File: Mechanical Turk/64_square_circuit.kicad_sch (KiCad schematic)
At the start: 82 parts, among them U1 LM2596S-ADJ

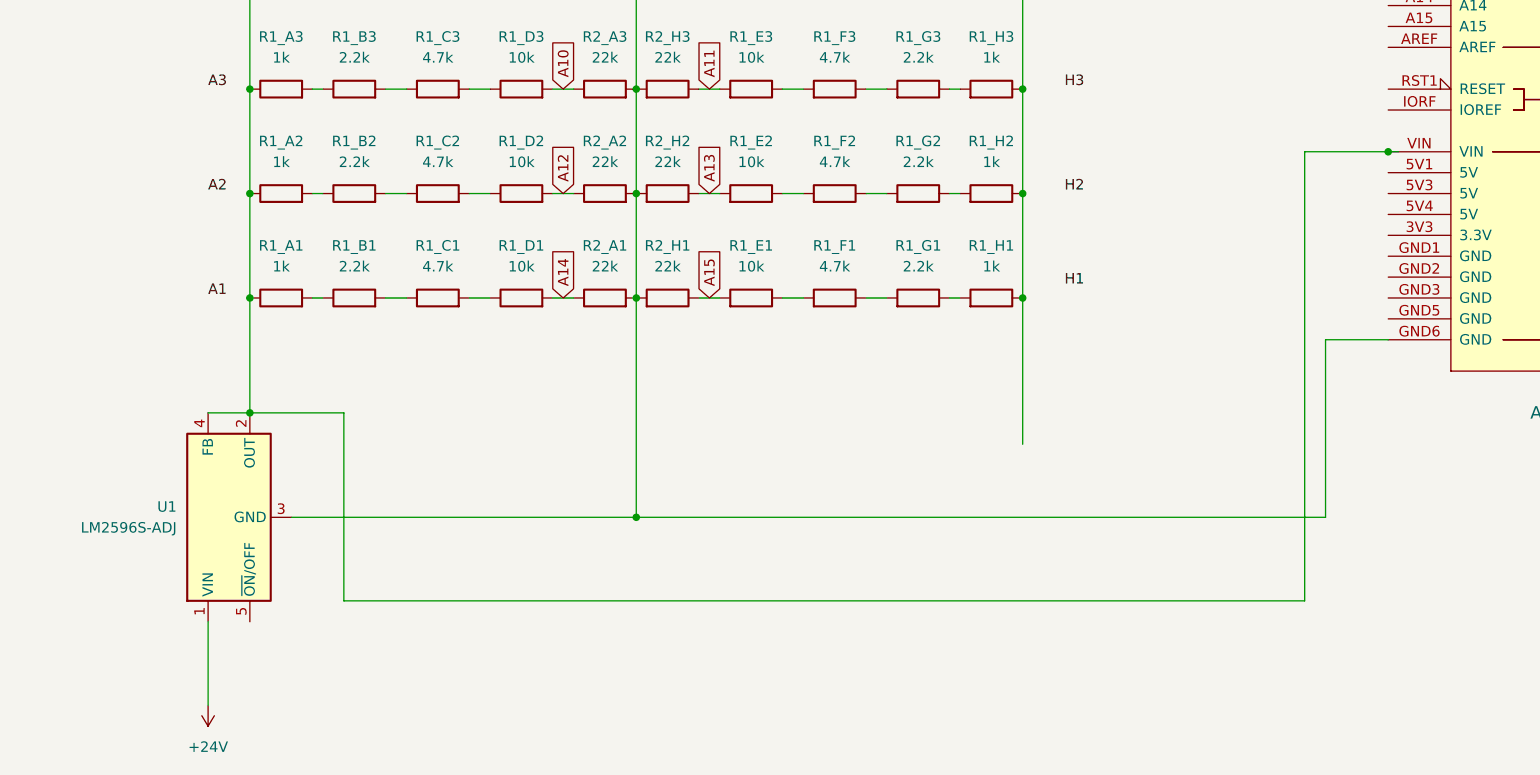
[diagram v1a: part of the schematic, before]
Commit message: gripper design is completed
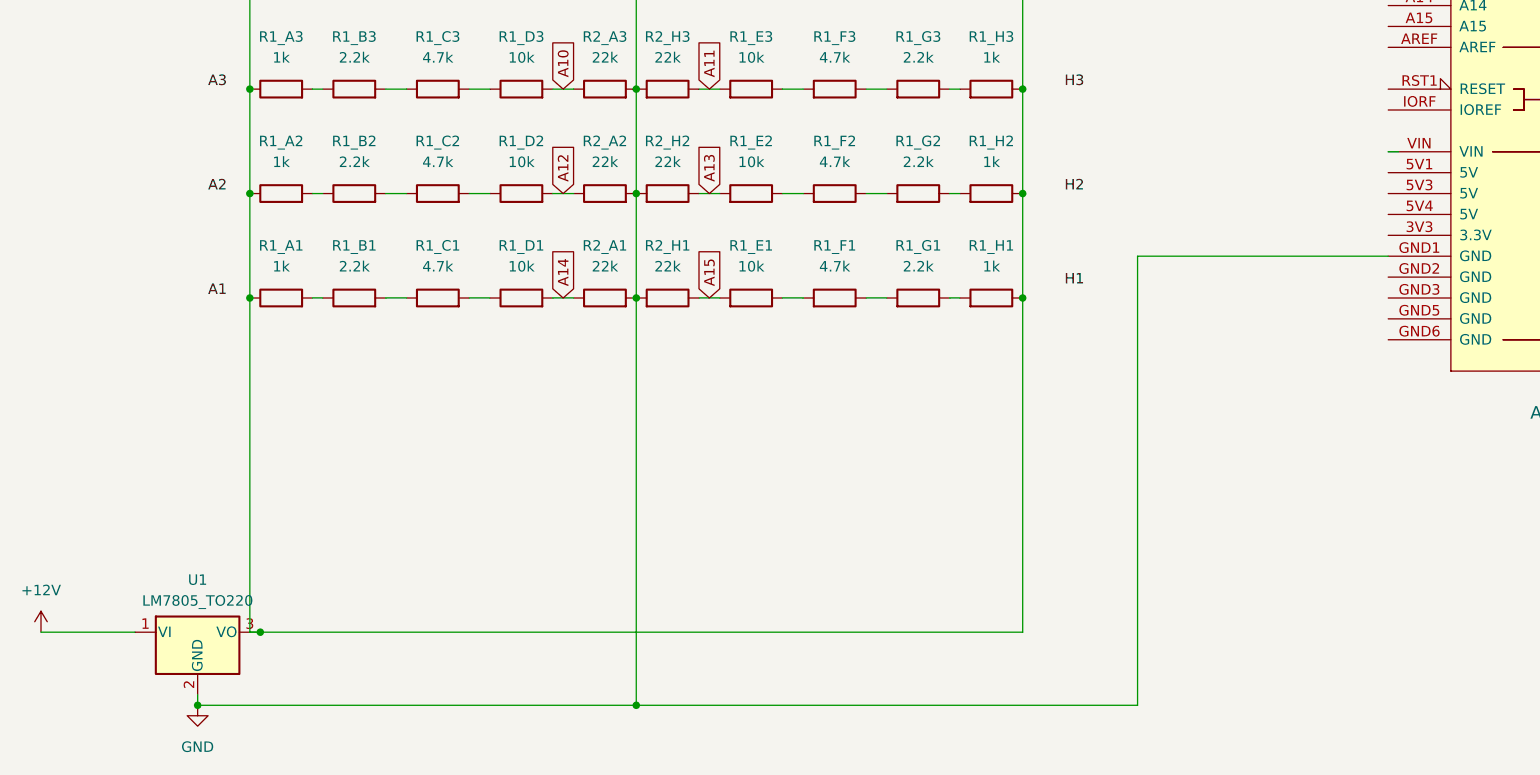
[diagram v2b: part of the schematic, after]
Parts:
- removed U1: LM2596S-ADJ, Package_TO_SOT_SMD:TO-263-5_TabPin3, symbol Regulator_Switching:LM2596S-ADJ
- added U1: LM7805_TO220, Package_TO_SOT_THT:TO-220-3_Vertical, symbol Regulator_Linear:LM7805_TO220
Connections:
- net at R1_A1.1, R1_A2.1, R1_A3.1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: now also U1.3 (VO); no longer A1.VIN
- net GND: now reaches R2_A1.2, R2_A2.2, R2_A3.2, R2_A4.2, R2_A5.2, R2_A6.2, R2_A7.2, R2_A8.2, R2_A8.2, R2_H1.2, R2_H2.2, R2_H3.2, R2_H4.2, R2_H5.2, R2_H6.2, R2_H8.2
- net GND: now also A1.GND1 (GND), U1.2 (GND); no longer A1.GND6 (GND)
- new net +12V: U1.1 (VI)
